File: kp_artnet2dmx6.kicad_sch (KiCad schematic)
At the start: 108 parts, among them IC1 KSZ8081MNXIA-TR, IC2 M95640-RMN6P, IC3 AP2281-3WG-7, IC4 MP2331HGTL-P, J1 RJ45_Amphenol_RJMG1BD3B8K1ANR, J10 DMX, J11 DMX, J12 DMX, J14 SWD, J15 USB-B-S-RA, J2 SCREEN, J3 BTN, J4 BTN, J5 BTN, J6 BTN, J7 DMX, J8 DMX, J9 DMX, Q1 AO3401A, SW1 SW_SPDT, U1 STM32F407VGT6, U2 MCP23S17_SP, U3 USBLC6-2SC6, Y1 ASDDV-25.000MHZ-LC-T

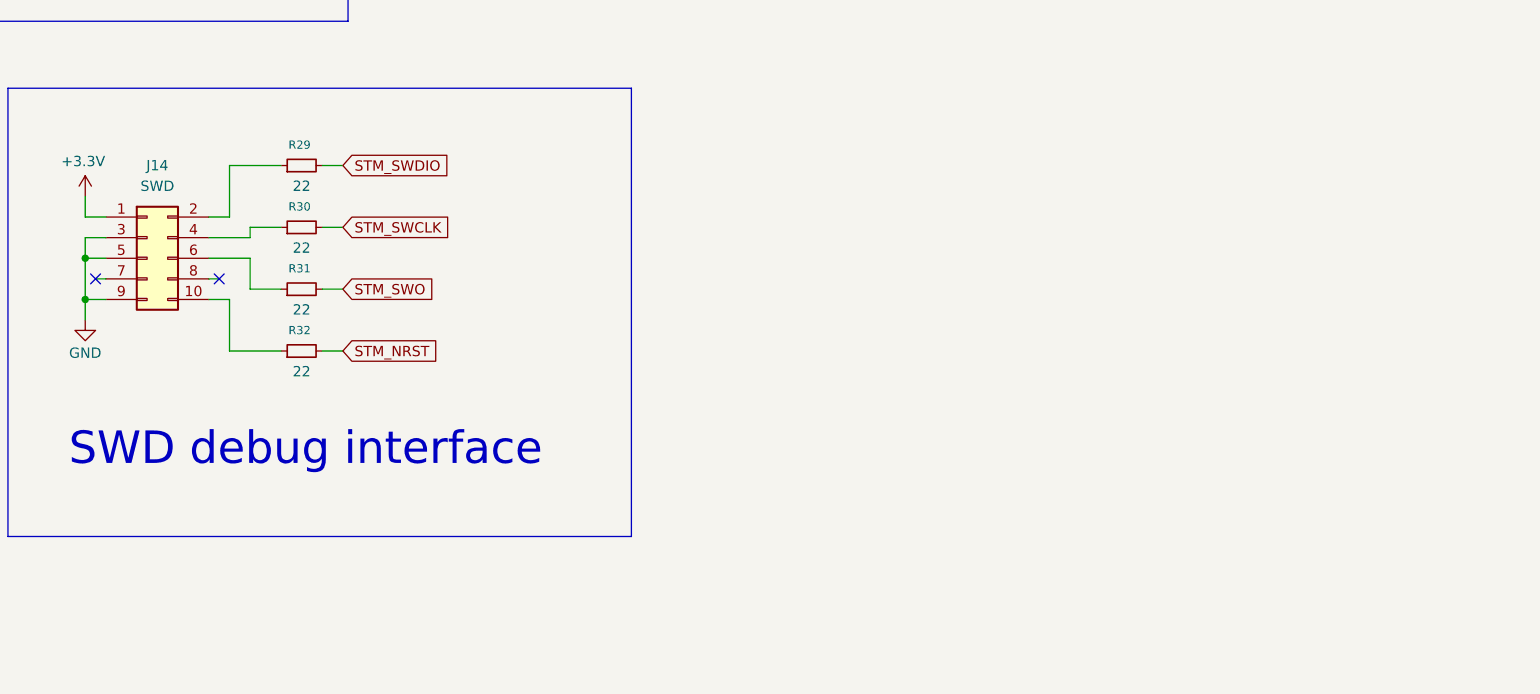
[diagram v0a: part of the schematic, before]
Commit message: start assigning netclasses
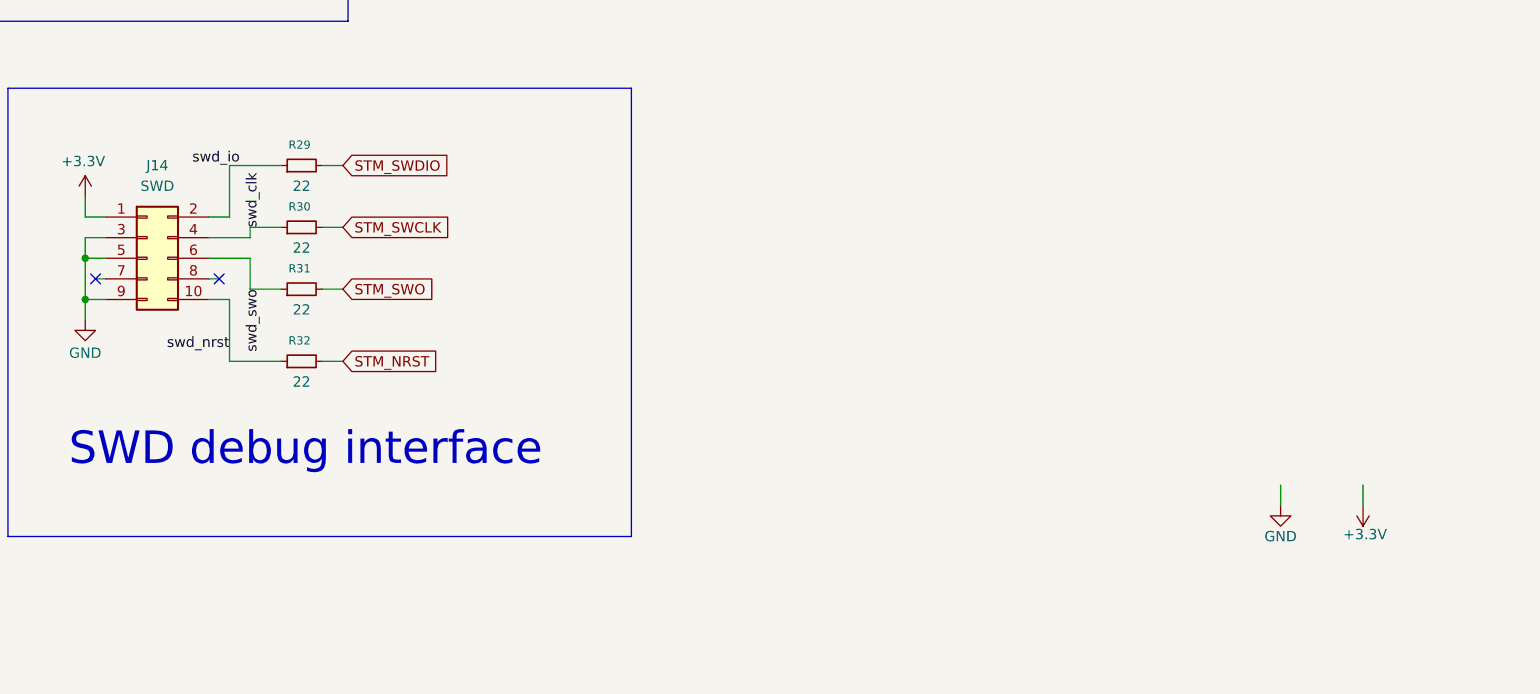
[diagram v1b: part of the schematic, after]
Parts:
- IC4: footprint SamacSys:MP2331HGTLP -> Package_TO_SOT_SMD:SOT-583-8
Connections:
- net swd_clk: now reaches J14.4 (Pin_4), R30.1
- net swd_io: now reaches J14.2 (Pin_2), R29.1
- net swd_nrst: now reaches J14.10 (Pin_10), R32.1
- net swd_swo: now reaches J14.6 (Pin_6), R31.1
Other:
- moved on the sheet: R32

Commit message: main pcb : everything is connected
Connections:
- net Earth: no longer J1.R8
- net GND: now also J1.R8
- net ksz_led1+: now reaches J1.L4, R6.2
- net mp2331_bst2: now reaches C39.2, R22.1
- net mp2331_bst1: now reaches IC4.5 (BST), R22.2
- net mp2331_fb2: now reaches C38.1, R23.2, R26.2, R28.1
- net mp2331_pg: now reaches C33.2, IC4.1 (PG)
- net mp2331_en: now reaches IC4.6 (EN), R27.1
- net ksz_led0+: now reaches J1.L1, R5.2
- net mp2331_ss: now reaches C34.2, IC4.7 (SS)
- net mp2331_fb1: now reaches IC4.8 (FB), R23.1
- net rj45_rct: now reaches C15.1, J1.R4 (TCT)
- net rj45_tct: now reaches C20.2, J1.R5 (RCT)
- net bootswitch: now reaches R1.2, SW1.2 (B)
- net usbmos2: now reaches FB4.1, Q1.2 (S)
- net usbmos1: now reaches F1.2, Q1.3 (D)
- net ksz_rext: now reaches IC1.10 (REXT), R3.2
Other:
- moved on the sheet: C15, C20, C33, C34, C38, C39, F1, R22, R23, R26, R27, R28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

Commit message: fix drc errors
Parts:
- removed TP1: testpoint, TestPoint:TestPoint_THTPad_1.5x1.5mm_Drill0.7mm, symbol Connector:TestPoint_Small
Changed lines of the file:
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@@
-	)
-	(symbol
-		(lib_id "Connector:TestPoint_Small")
-		(at 95.25 367.03 0)
-		(unit 1)
-		(body_style 1)
-		(exclude_from_sim no)
-		(in_bom no)
-		(on_board yes)
-		(in_pos_files yes)
-		(dnp no)
-		(fields_autoplaced yes)
-		(property "Reference" "TP1"
-			(at 96.52 365.7599 0)
-			(show_name no)
-			(do_not_autoplace no)
-			(effects
-				(font
-					(size 1.27 1.27)
-				)
-				(justify left)
-			)
-		)
-		(property "Value" "testpoint"
-			(at 96.52 368.2999 0)
-			(show_name no)
-			(do_not_autoplace no)
-			(effects
-				(font
-					(size 1.27 1.27)
-				)
-				(justify left)
-			)
-		)
-		(property "Footprint" "TestPoint:TestPoint_THTPad_1.5x1.5mm_Drill0.7mm"
-			(at 100.33 367.03 0)
-			(hide yes)
-			(show_name no)
-			(do_not_autoplace no)
-			(effects
-				(font
-					(size 1.27 1.27)
-				)
-			)
-		)
-		(property "Datasheet" ""
-			(at 100.33 367.03 0)
-			(hide yes)
-			(show_name no)
-			(do_not_autoplace no)
-			(effects
-				(font
-					(size 1.27 1.27)
-				)
-			)
-		)
-		(property "Description" "test point"
-			(at 95.25 367.03 0)
-			(hide yes)
-			(show_name no)
-			(do_not_autoplace no)
-			(effects
-				(font
-					(size 1.27 1.27)
-				)
-			)
-		)
-		(pin "1"
-		)
-		(instances
-			(project "kp_artnet2dmx6"
-				(path "/c020d59c-a220-4a4b-a853-32d85708743c"
-					(reference "TP1")
-					(unit 1)
-				)
-			)
-		)
 	)
 	(symbol

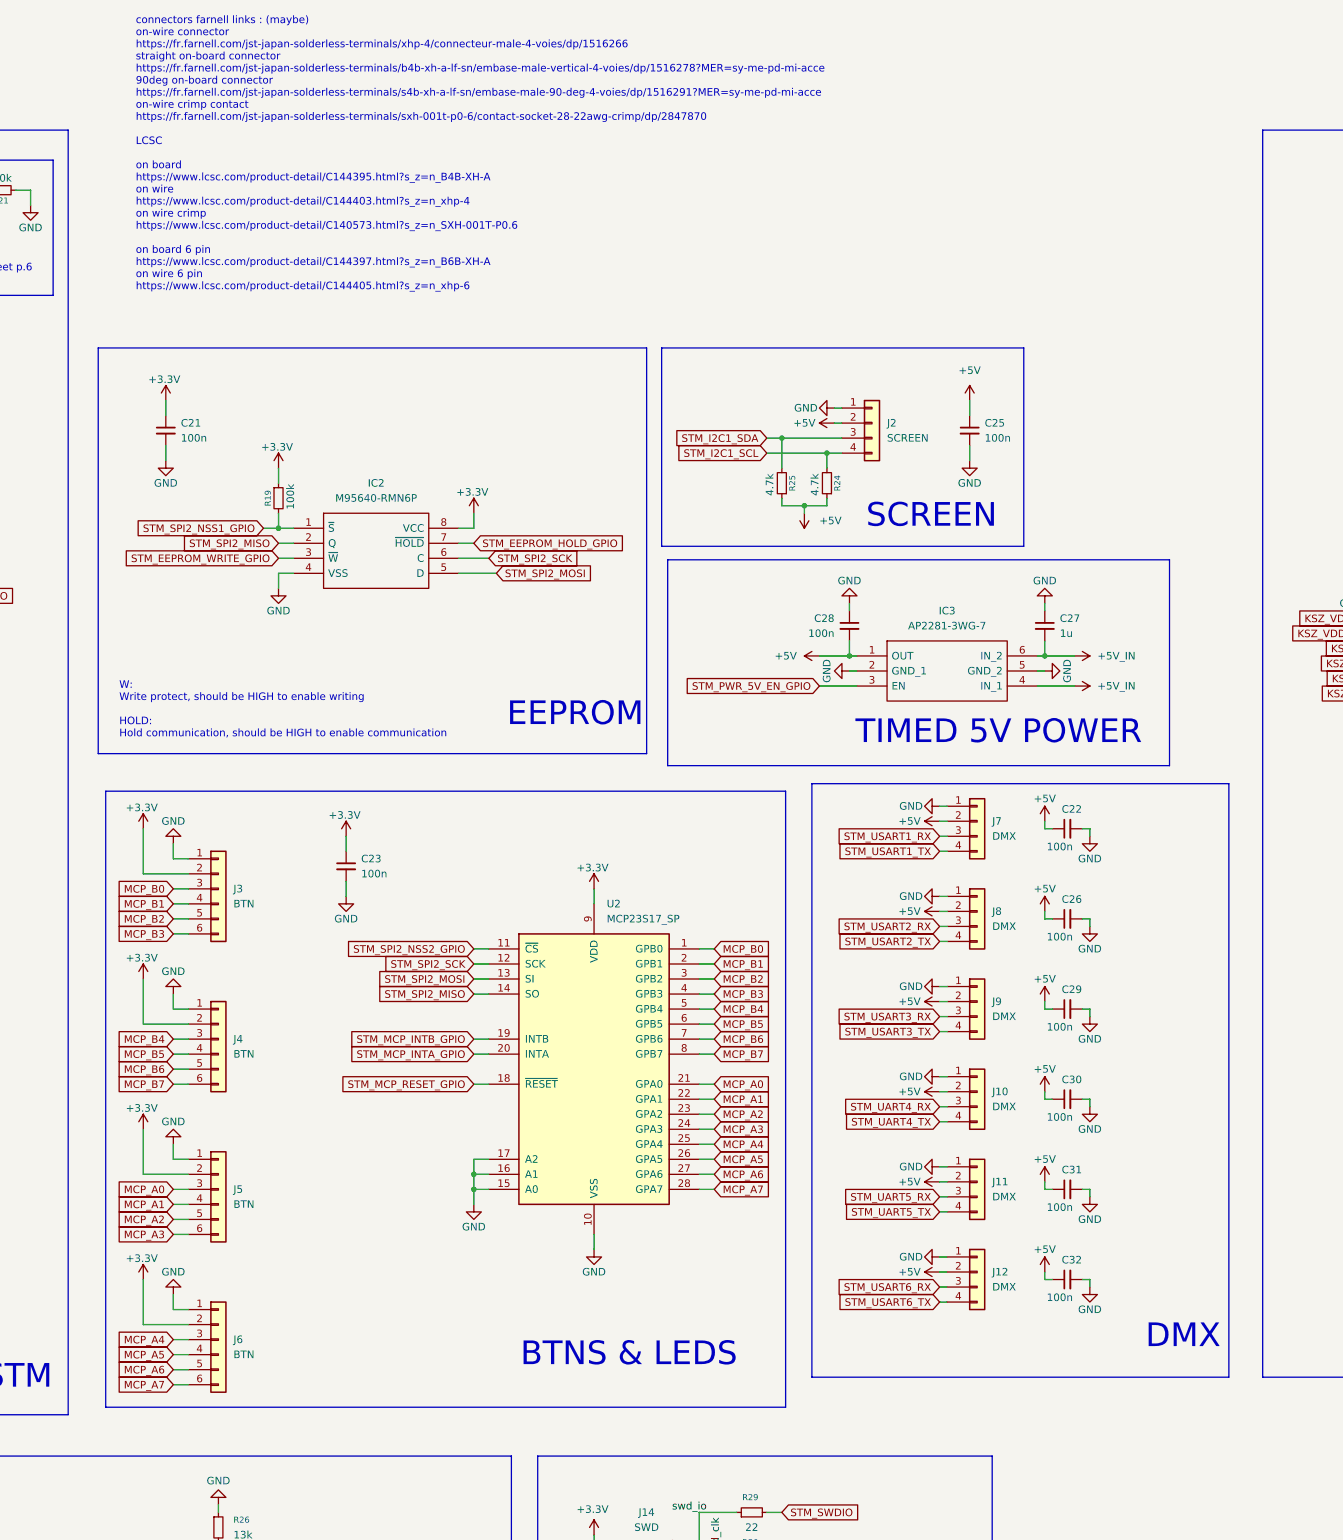
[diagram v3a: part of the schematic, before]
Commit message: schematic: change connectors from jst xh to IDC
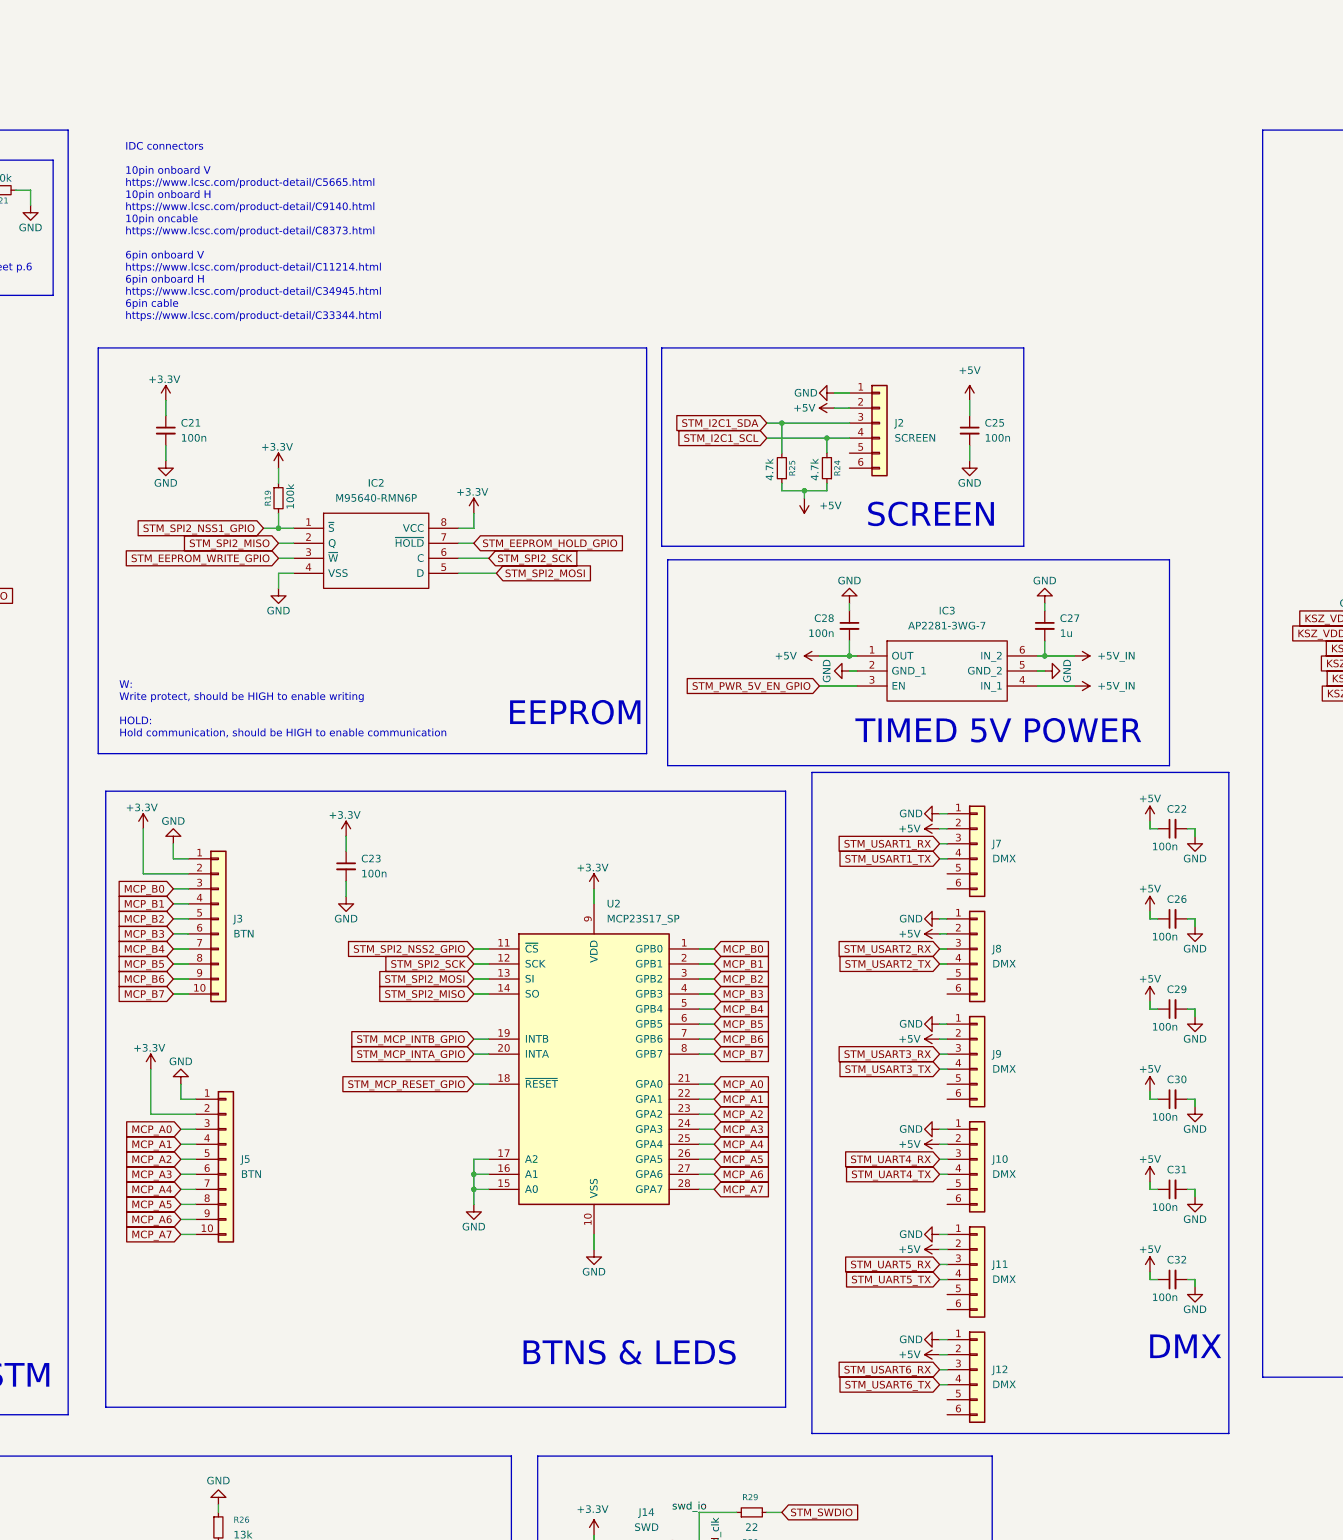
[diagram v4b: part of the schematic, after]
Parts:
- removed J4, J6: BTN, Connector_JST:JST_XH_B6B-XH-A_1x06_P2.50mm_Vertical, symbol Connector_Generic:Conn_01x06
- J10, J11, J12, J2, J7, J8, J9: footprint Connector_JST:JST_XH_B4B-XH-A_1x04_P2.50mm_Vertical -> Connector_IDC:IDC-Header_2x03_P2.54mm_Vertical; symbol Connector_Generic:Conn_01x04 -> Connector_Generic:Conn_01x06
- J3, J5: footprint Connector_JST:JST_XH_B6B-XH-A_1x06_P2.50mm_Vertical -> Connector_IDC:IDC-Header_2x05_P2.54mm_Vertical; symbol Connector_Generic:Conn_01x06 -> Connector_Generic:Conn_01x10
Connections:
- net MCP_A4: now also J5.7 (Pin_7)
- net MCP_A5: now also J5.8 (Pin_8)
- net MCP_A6: now also J5.9 (Pin_9)
- net MCP_A7: now also J5.10 (Pin_10)
- net MCP_B4: now also J3.7 (Pin_7)
- net MCP_B5: now also J3.8 (Pin_8)
- net MCP_B6: now also J3.9 (Pin_9)
- net MCP_B7: now also J3.10 (Pin_10)
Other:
- note added: "IDC connectors 10pin onboard V https://www.lcsc.com/product-detail/C5665.html 10pin onboard H https://www.lcsc.com/product-detail/C9140.html 10pin oncable https://www.lcsc.com/product-detail/C8373.html 6pin onboard V https://www.lcsc.com/product-detail/C11214.html 6pin onboard H https://www.lcsc.com/product-detail/C34945.html 6pin cable https://www.lcsc.com/product-detail/C33344.html"
- note removed: "connectors farnell links : (maybe) on-wire connector https://fr.farnell.com/jst-japan-solderless-terminals/xhp-4/connecteur-male-4-voies/dp/1516266 straight on-board connector https://fr.farnell.com/jst-japan-solderless-terminals/b4b-xh-a-lf-sn/embase-male-vertical-4-voies/dp/1516278?MER=sy-me-pd-mi-acce 90deg on-board connector https://fr.farnell.com/jst-japan-solderless-terminals/s4b-xh-a-lf-sn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"
- moved on the sheet: C22, C26, C29, C30, C31, C32, R24, R25

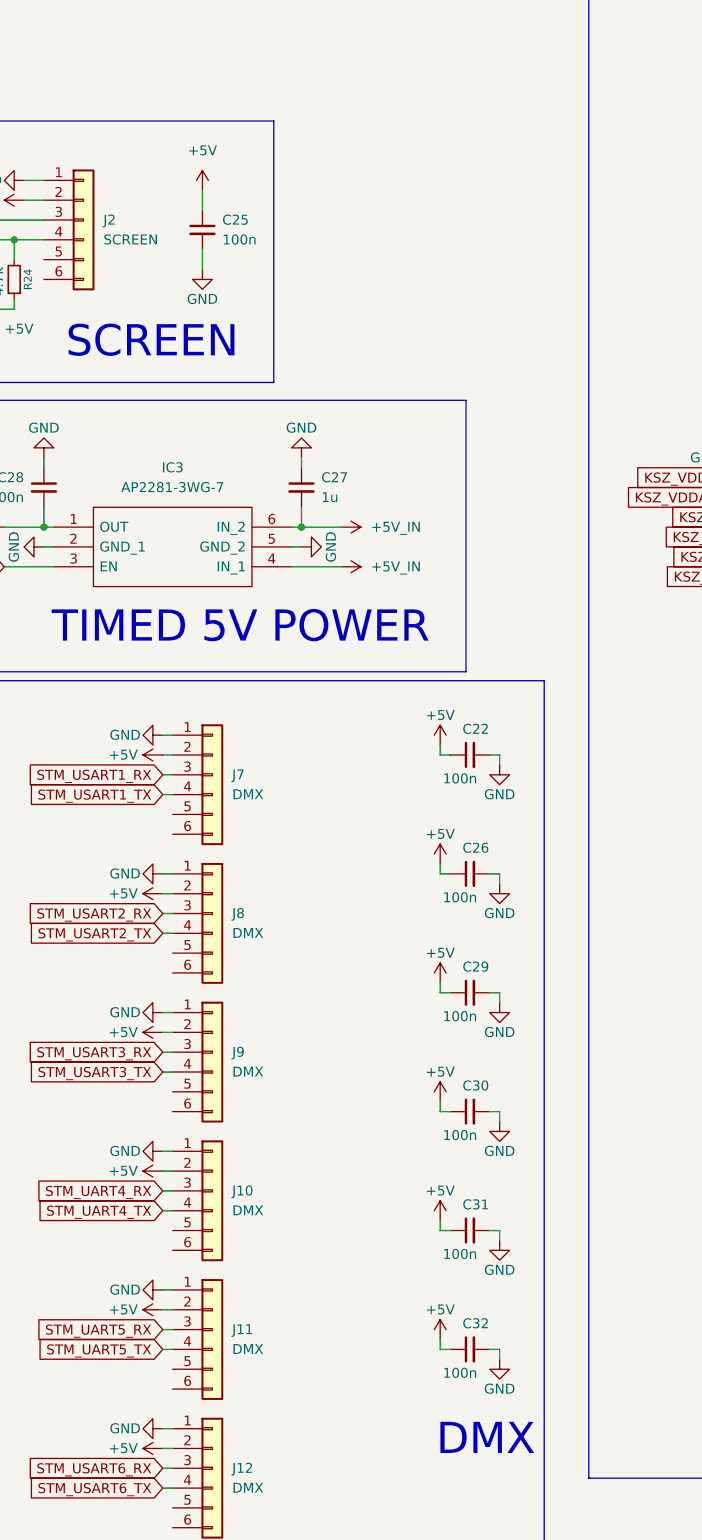
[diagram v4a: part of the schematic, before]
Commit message: sch: remove caps on connectors
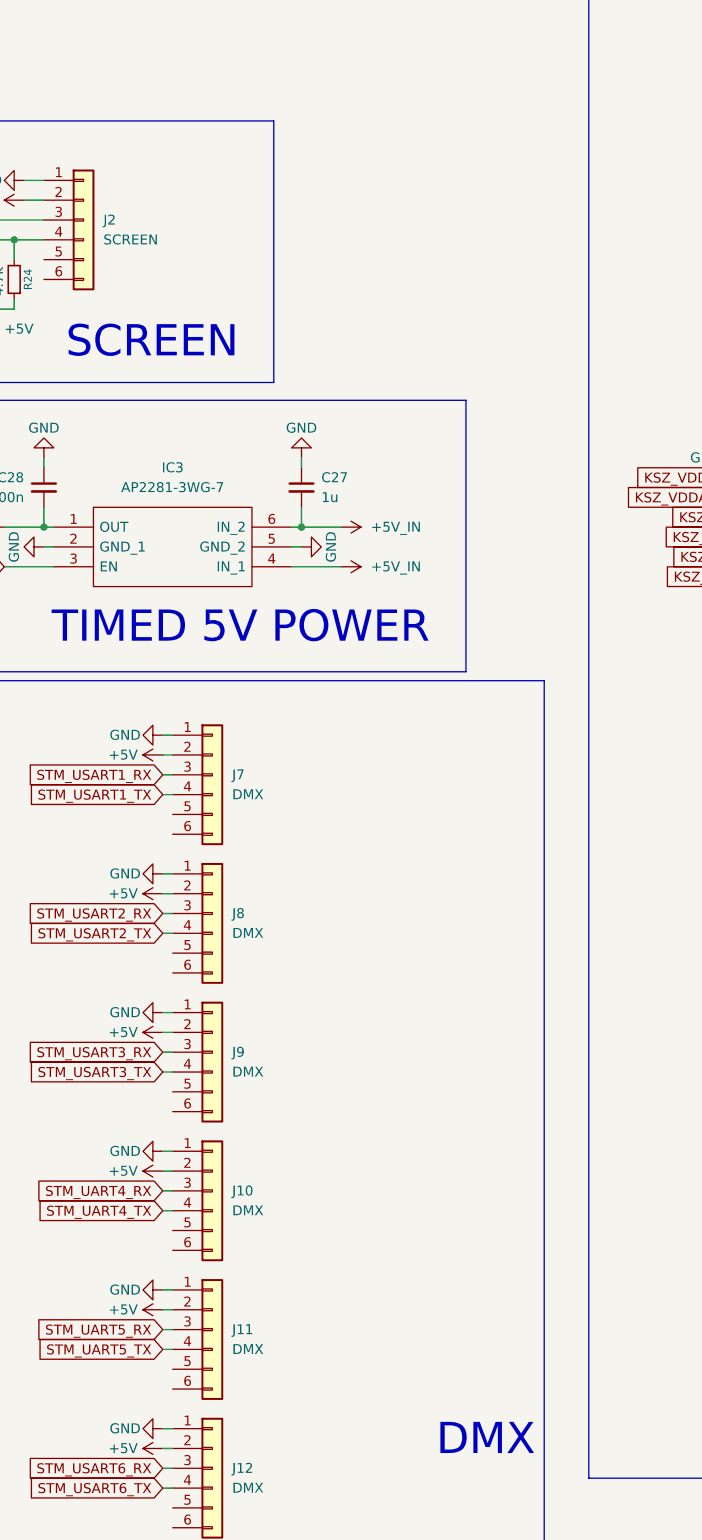
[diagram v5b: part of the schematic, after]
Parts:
- removed C22, C25, C26, C29, C30, C31, C32: 100n, Capacitor_SMD:C_0402_1005Metric, symbol Device:C_Small
